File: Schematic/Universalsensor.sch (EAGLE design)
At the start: 26 parts, among them IC1 MEGA328P-AU, IC2 DS18B20, IC3 DHT-22, IC4 SHT1X, IC5 MAX1724

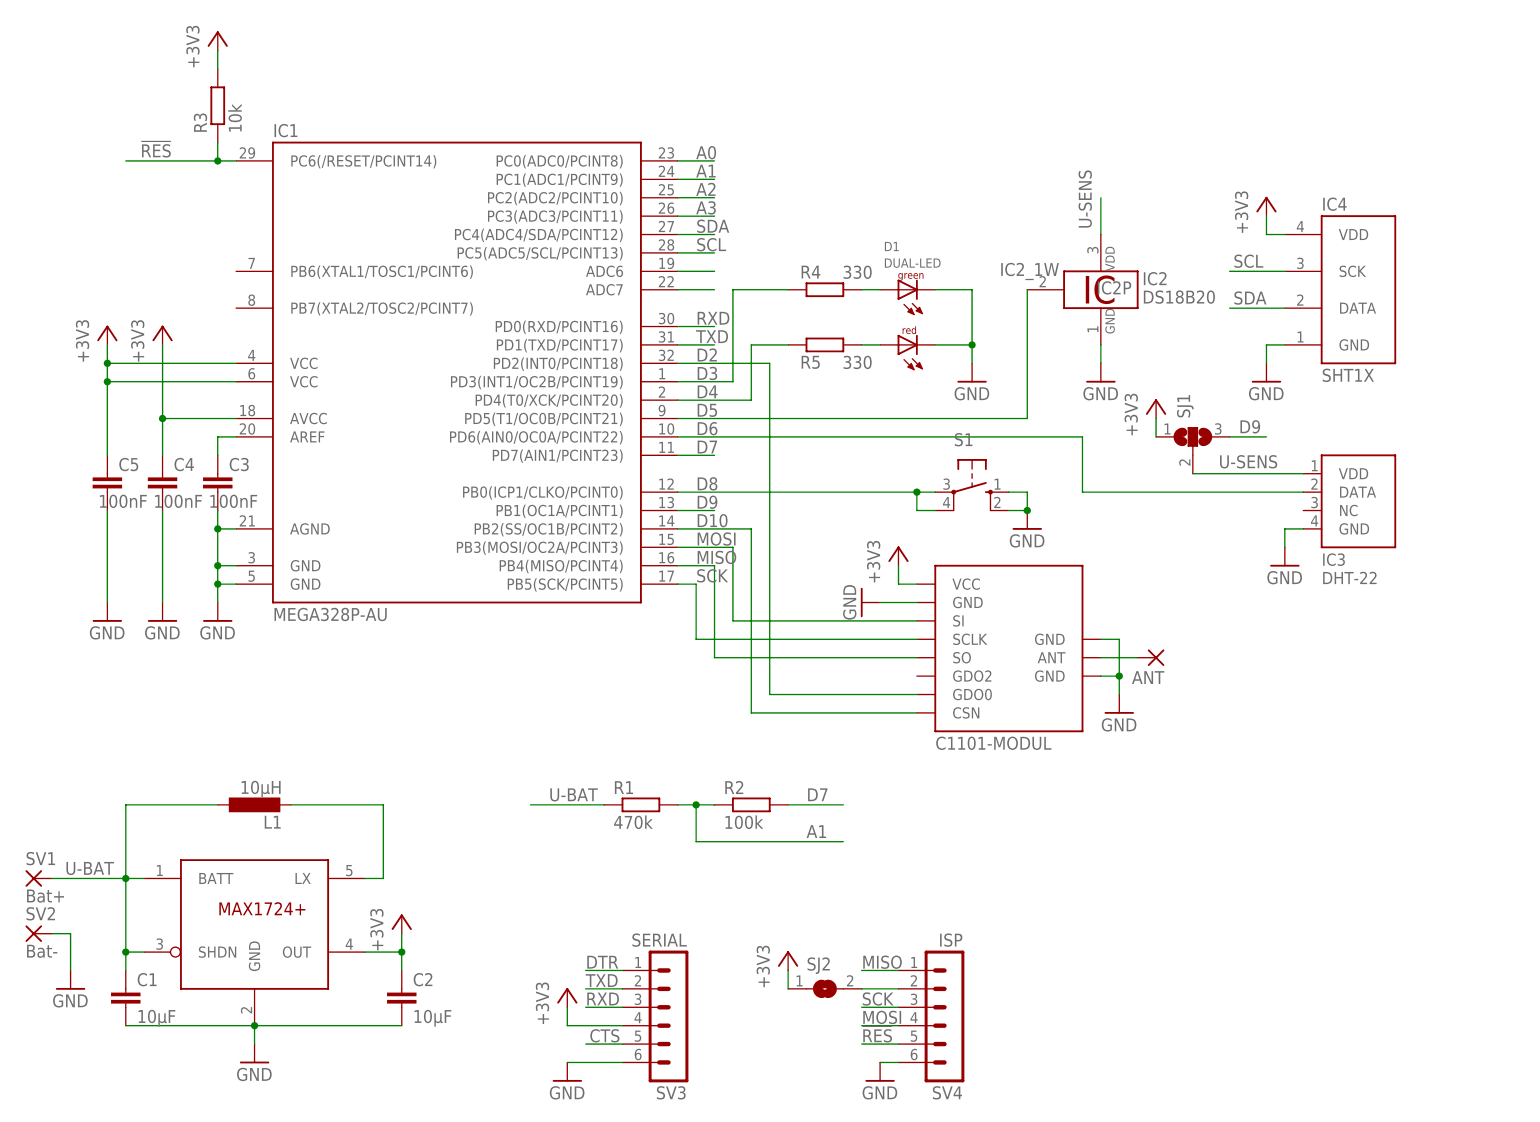
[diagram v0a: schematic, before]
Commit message: new schematic for low freq crystal oscillator and sht21
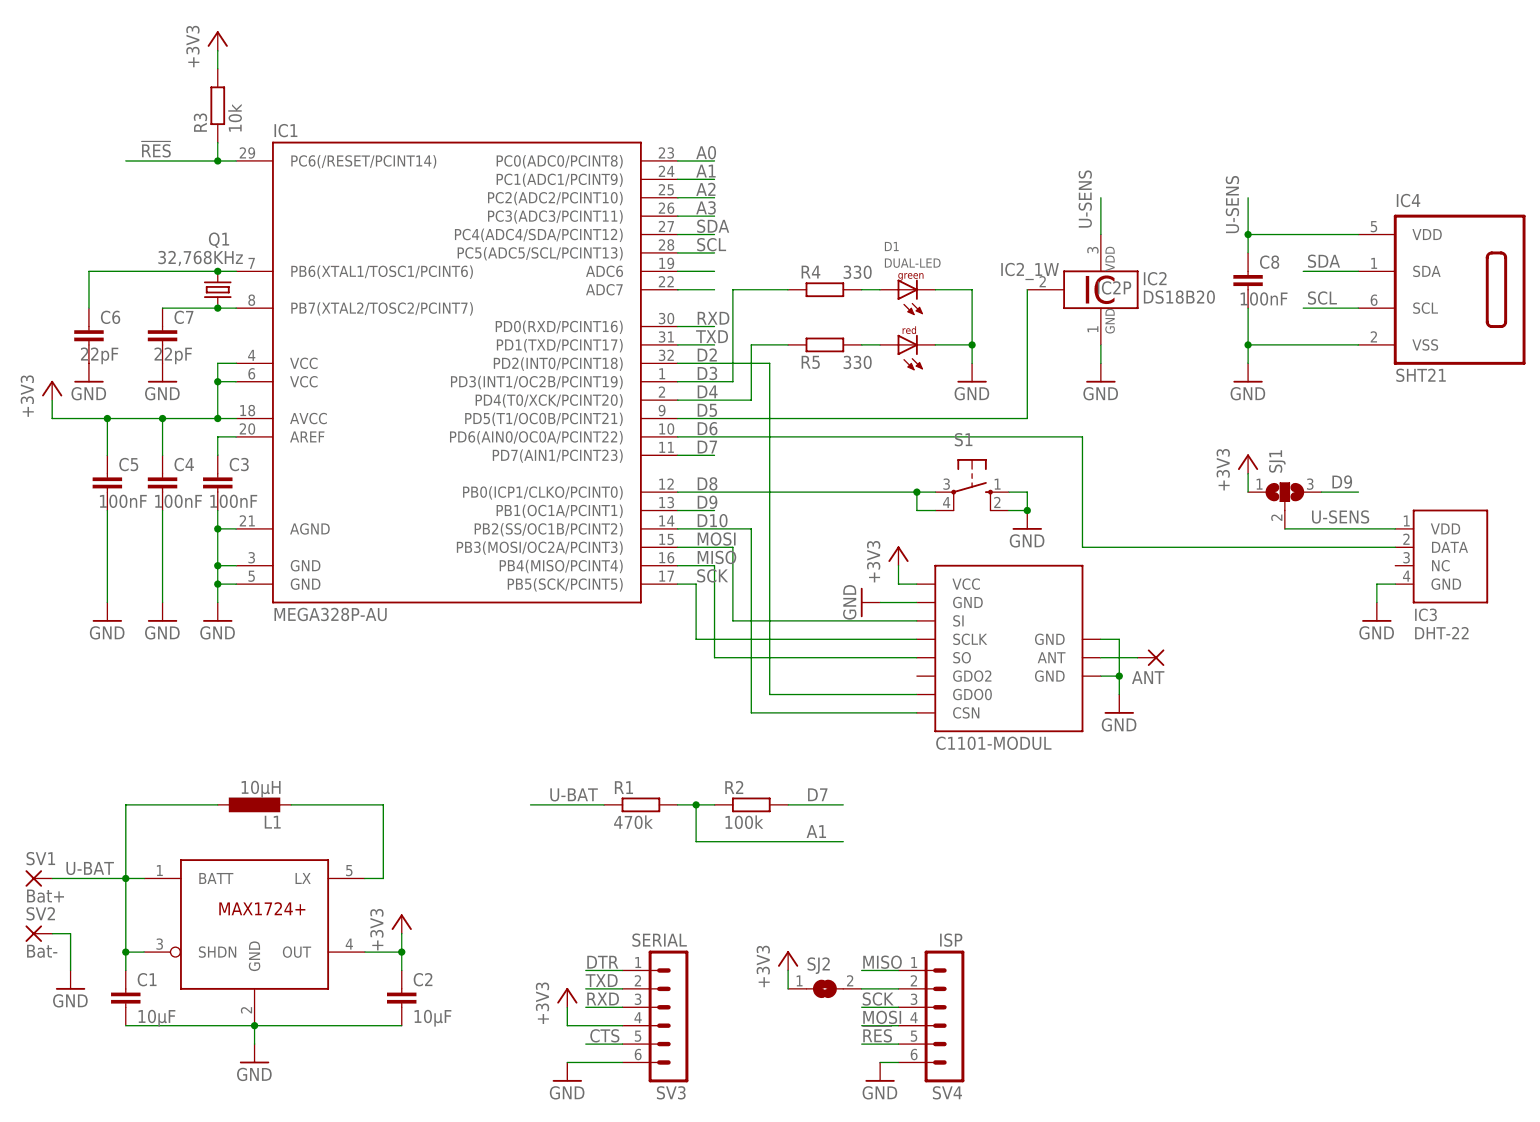
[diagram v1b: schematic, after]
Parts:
- added C6, C7: 22pF, rcl:C-EUC0603K
- added C8: 100nF, rcl:C-EUC0603K
- added Q1: 32,768KHz, kanflo:OSCILLATOR_32KHZ
- IC4: value SHT1X -> SHT21; device sht10_11_15:SHT1X -> sensirion:SHT21
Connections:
- new net N$3: C6.1, IC1.PB6(XTAL1/TOSC1/PCINT6), Q1.2
- new net N$8: C7.1, IC1.PB7(XTAL2/TOSC2/PCINT7), Q1.1
- net +3V3: no longer IC4.VDD
- net GND: now also C6.2, C7.2, C8.2, IC4.VSS; no longer IC4.GND
- net SCL: now also IC4.SCL; no longer IC4.SCK
- net SDA: now also IC4.SDA; no longer IC4.DATA
- net U-SENS: now also C8.1, IC4.VDD
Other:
- moved on the sheet: IC3, SJ1

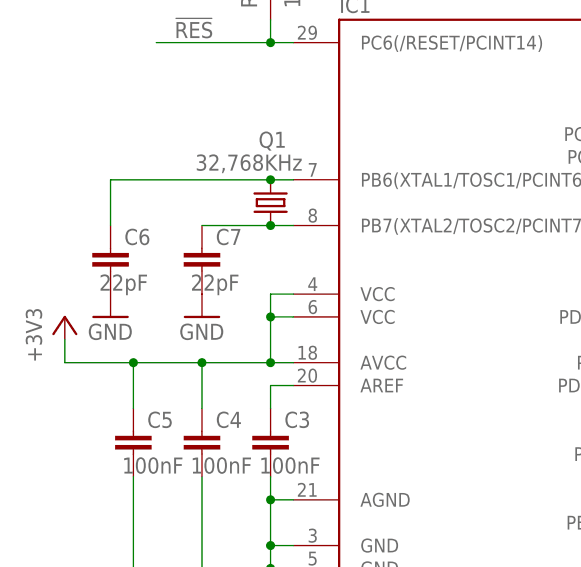
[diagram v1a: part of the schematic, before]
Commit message: schematic changed - only one crystal load capacitor needed, crystal doc added
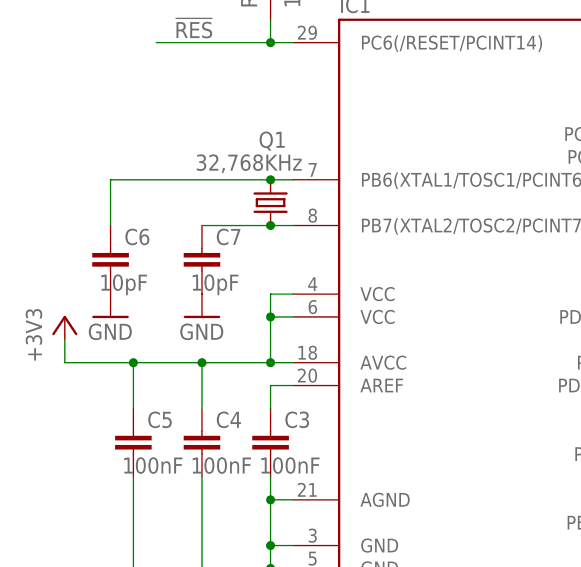
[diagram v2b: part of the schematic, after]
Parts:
- C6, C7: value 22pF -> 10pF
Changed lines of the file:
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@@
 </attributes>
 <variantdefs>
-<variantdef name="DHT-22"/>
-<variantdef name="SHT-11"/>
+<variantdef name="DHT-22" current="yes"/>
+<variantdef name="SHT-21"/>
 </variantdefs>
 <classes>
@@
 <part name="GND9" library="supply1" deviceset="GND" device=""/>
 <part name="IC3" library="Pn-Lib" deviceset="DHT-22" device="">
-<variant name="SHT-11" populate="no"/>
+<variant name="SHT-21" populate="no"/>
 </part>
 <part name="GND10" library="supply1" deviceset="GND" device=""/>
@@
 <part name="GND14" library="supply1" deviceset="GND" device=""/>
 <part name="Q1" library="kanflo" deviceset="OSCILLATOR_32KHZ" device="" value="32,768KHz"/>
-<part name="C6" library="rcl" deviceset="C-EU" device="C0603K" value="22pF"/>
-<part name="C7" library="rcl" deviceset="C-EU" device="C0603K" value="22pF"/>
+<part name="C6" library="rcl" deviceset="C-EU" device="C0603K" value="10pF">
+<variant name="DHT-22" populate="no"/>
+<variant name="SHT-21" populate="no"/>
+</part>
+<part name="C7" library="rcl" deviceset="C-EU" device="C0603K" value="10pF"/>
 <part name="+3V4" library="supply1" deviceset="+3V3" device=""/>
 <part name="GND15" library="supply1" deviceset="GND" device=""/>
 <part name="GND16" library="supply1" deviceset="GND" device=""/>
-<part name="IC4" library="sensirion" deviceset="SHT21" device=""/>
+<part name="IC4" library="sensirion" deviceset="SHT21" device="">
+<variant name="DHT-22" populate="no"/>
+</part>
 <part name="C8" library="rcl" deviceset="C-EU" device="C0603K" value="100nF"/>
 </parts>
